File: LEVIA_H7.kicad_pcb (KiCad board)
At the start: 6 copper layers, 36.5 x 36.5 mm, 145 parts, among them J1 TF-028-H265, Q1 AO3400A, SW2 RKCGG140SMTRLFS, U1 USBLC6-2P6, U10 ZX-SH1.0-4PWT, U11 ZX-SH1.0-3PWT, U12 SIT1051TK/3, U13 ZX-SH1.0-4PWT, U14 ICM-42688-P, U15 ICM-42688-P, U16 DPS368XTSA1, U17 IST8310, U18 ZX-SH1.0-4PWT, U19 ZX-SH1.0-6PWT, U2 STM32H743VIHx, U20 ZX-SH1.0-6PWT, U21 ZX-SH1.0-3PWT, U22 ZX-SH1.0-8PWT, U24 ZX-SH1.0-4PWT, U25 BME680, U3 ZX-SH1.0-4PWT, U4 LMR43620R5RPER, U5 LMR604303SRAKRQ1, U6 AP7361C-33FGE-7, U7 AP7361C-33FGE-7, U8 ZX-SH1.0-4PWT, U9 AT7456ELAH, Y1 8MHz, Y2 XL7EL89COI-111YLC-27M

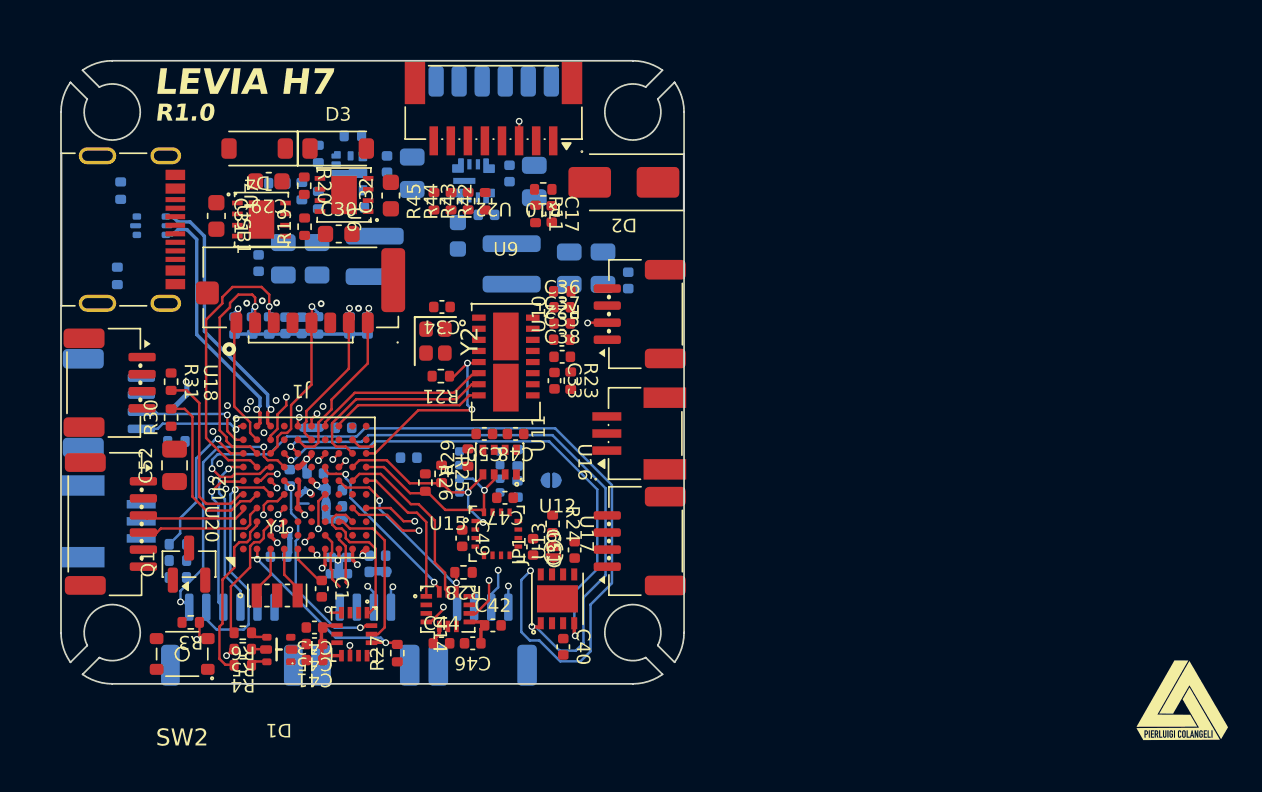
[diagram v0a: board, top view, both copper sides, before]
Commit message: new PCB custom outline
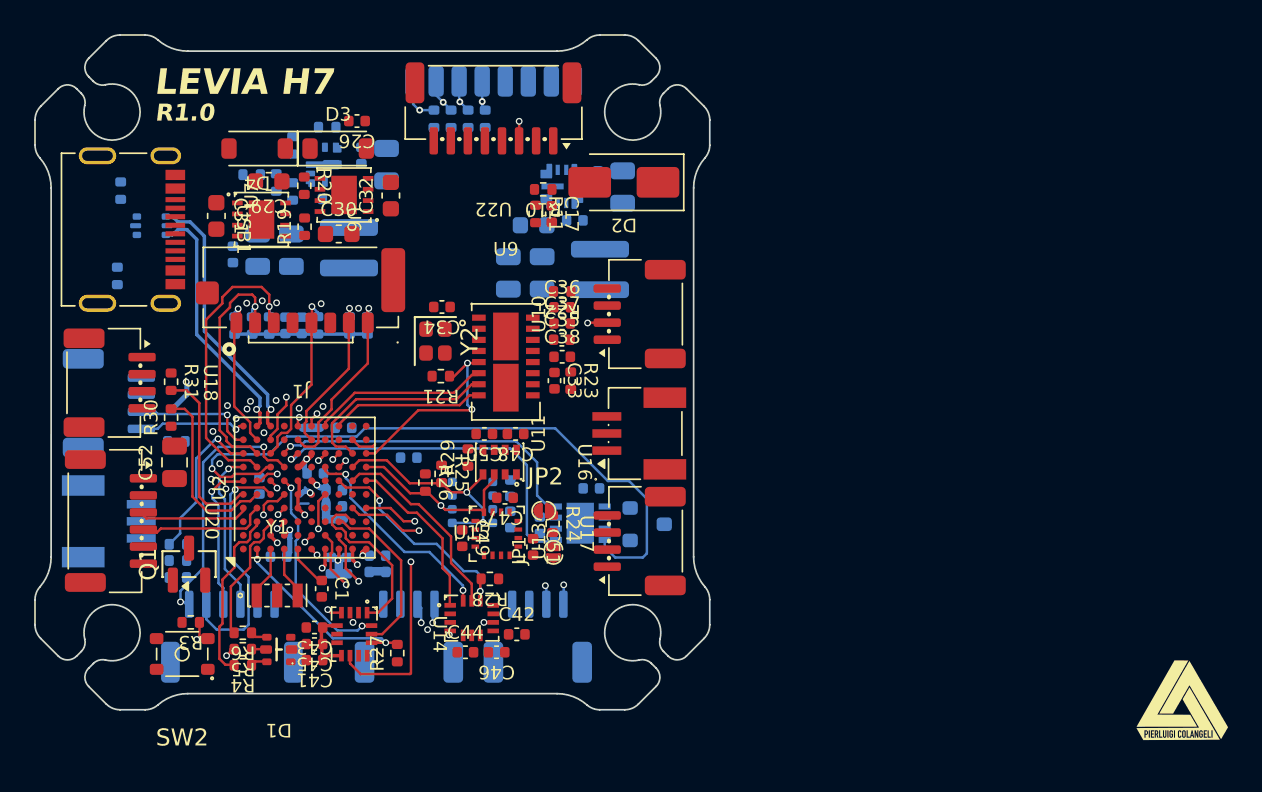
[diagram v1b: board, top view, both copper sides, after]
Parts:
- added D6: PESD2CAN, PCM_Package_TO_SOT_SMD_AKL:SOT-23, B.Cu at (154.8, 78.0)
- C26, JP2: moved to F.Cu
- C39, C40, R42, R43, R44, R45, U12: moved to B.Cu
- moved C26 18.4 mm to (137.8, 54.4), turned to 180 degrees
- moved C40 7.26 mm to (148.5, 78.1)
- moved C22 5.55 mm to (146.7, 63.3)
- moved C13 5.19 mm to (153.4, 58.3)
- moved L1 5.19 mm to (152.0, 63.1)
- moved U4 5.19 mm to (149.8, 58.2)
- moved C15 5.19 mm to (151.9, 57.8)
- moved C20 5.19 mm to (150.6, 60.2)
- moved R42 4.83 mm to (145.3, 54.3), turned to -90 degrees
- moved R44 4.83 mm to (143.3, 54.3), turned to -90 degrees
- moved R45 4.83 mm to (142.3, 54.3), turned to -90 degrees
- moved R43 4.82 mm to (144.3, 54.3), turned to -90 degrees
- moved U12 4.63 mm to (150.9, 77.9), turned to 90 degrees
- moved C18 4.48 mm to (148.2, 60.5), turned to 180 degrees
- moved C39 3.74 mm to (151.5, 75.9), turned to 180 degrees
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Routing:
- net /MCU/MOTOR3: track 3.42 -> 37.2 mm, vias 0 -> 2
- net /MCU/MOTOR4: track 3.13 -> 35.6 mm, vias 0 -> 2
- net /MCU/MOTOR1: track 4.44 -> 35.4 mm, vias 1 -> 2
- net /MCU/MOTOR2: track 3.17 -> 33.5 mm, vias 1 -> 2
- net /CAN/CAN1.TX: track 34.5 -> 20.7 mm, vias 2 -> 1
- net /CAN/CAN1.RX: track 30.0 -> 18.7 mm, vias 2 -> 1
- net /CAN/CAN1.SILENT: track 49.0 -> 38.8 mm, vias 2 -> 1
- net /MCU/GYRO1_CLKIN: track 15.5 -> 19.2 mm
- net +3V3_SENS: track 7.51 -> 4.25 mm
- net /MCU/UART2.RX: track 11.6 -> 14.6 mm
- net /MCU/UART2.TX: track 13.5 -> 16.5 mm
- net /MCU/UART6.RX: track 18.3 -> 20.8 mm
- net /MCU/SPI4.CS: track 10.9 -> 13.2 mm
- net /MCU/SPI4.MOSI: track 10.7 -> 12.6 mm
- net /MCU/I2C2.SCL: track 12.3 -> 13.6 mm
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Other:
- board size 36.5 x 36.5 mm -> 39.5 x 39.5 mm

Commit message: save
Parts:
- added REF**: KiCad-Logo2_5mm_SilkScreen, Symbol:KiCad-Logo2_5mm_SilkScreen, B.Cu at (139.1, 70.4)
- added REF**: OSHW-Logo_5.7x6mm_SilkScreen, Symbol:OSHW-Logo_5.7x6mm_SilkScreen, B.Cu at (129.4, 54.0)
- R42, R43, R44, R45: moved to F.Cu
- moved JP1 4.44 mm to (151.1, 75.6), turned to -90 degrees
- moved U11 3.40 mm to (154.6, 69.3)
- moved C13 2.90 mm to (150.5, 58.3)
- moved C15 2.90 mm to (149.0, 57.8)
- moved C18 2.90 mm to (145.3, 60.5)
- moved C20 2.90 mm to (147.7, 60.2)
- moved C22 2.90 mm to (143.8, 63.3)
- moved C24 2.90 mm to (145.8, 63.3)
- moved L1 2.90 mm to (149.1, 63.1)
- moved U4 2.90 mm to (146.9, 58.2)
- moved R44 2.75 mm to (142.7, 56.9), turned to 90 degrees
- moved R45 2.75 mm to (141.7, 56.9), turned to 90 degrees
- moved R42 2.75 mm to (144.7, 56.9), turned to 90 degrees
- moved R43 2.75 mm to (143.7, 56.9), turned to 90 degrees
- moved U10 2.61 mm to (154.6, 63.1)
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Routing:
- net /MCU/UART8.RX: track 43.5 -> 34.8 mm, vias 1 -> 2
- net /MCU/MOTOR2: track 33.5 -> 41.2 mm
- net /MCU/MOTOR1: track 35.4 -> 42.9 mm
- net /MCU/UART2.RX: track 14.6 -> 22.0 mm
- net /MCU/UART2.TX: track 16.5 -> 23.9 mm
- net /MCU/MOTOR3: track 37.2 -> 42.7 mm
- net /MCU/MOTOR4: track 35.6 -> 41.0 mm
- net +5V_SYS: track 0.00 -> 5.02 mm
- net /MCU/ADC1_VBAT1: track 48.9 -> 44.7 mm, vias 1 -> 2
- net Net-(U9-CLKIN): track 0.00 -> 3.38 mm
- net /ANALOG VTX/UART1.TX: track 23.5 -> 26.3 mm
- net /I2C1|SPI3/I2C1.SCL: track 10.6 -> 13.0 mm
- net /I2C1|SPI3/I2C1.SDA: track 10.4 -> 12.6 mm
- net Net-(U9-XFB): track 0.00 -> 2.05 mm
- net Net-(C36-Pad2): track 0.00 -> 2.03 mm
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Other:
- board text removed: "ADCs"
- board text removed: "BOOT"
- board text removed: "BUZZ"
- board text removed: "CAN-FD"
- board text removed: "DIGI VTX"
- board text removed: "I2C/SPI"
- board text removed: "JTAG"
- board text removed: "LDOS"
- board text removed: "LEDS"
- board text removed: "MOTORS"
- board text removed: "OSD"
- board text removed: "S E N S O R S"
- board text removed: "SD-CARD"
- board text removed: "SWITCHING REGS"
- board text removed: "UARTS"
- board text removed: "VTX"

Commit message: power routing
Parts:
- removed NT2, NT3, NT4, NT5: NetTie_2, NetTie:NetTie-2_SMD_Pad0.5mm
- added FB1: 600Ω@100MHz, Inductor_SMD:L_0402_1005Metric, B.Cu at (137.8, 80.1)
- added TP11: TestPoint, TestPoint:TestPoint_Pad_D1.0mm, B.Cu at (134.3, 75.5)
- R42, R43, R44, R45: moved to B.Cu
- moved NT1 24.8 mm to (128.3, 58.4)
- moved C9 5.24 mm to (136.5, 77.1), turned to 0 degrees
- moved C2 3.37 mm to (137.6, 78.0), turned to 180 degrees
- moved R42 1.91 mm to (144.7, 55.0)
- moved R43 1.91 mm to (143.7, 55.0)
- moved R44 1.91 mm to (142.7, 55.0)
- moved R45 1.91 mm to (141.7, 55.0)
- moved C12 1.90 mm to (133.7, 76.8), turned to 180 degrees
- moved C4 1.82 mm to (137.6, 78.9), turned to 180 degrees
- moved C8 1.55 mm to (136.1, 73.6)
- moved C5 1.55 mm to (136.2, 78.9), turned to 90 degrees
- moved C7 1.48 mm to (137.9, 76.3), turned to -90 degrees
- moved C3 1.06 mm to (136.2, 80.7)
- moved C6 0.97 mm to (134.0, 79.3), turned to -90 degrees
- moved C10 0.80 mm to (136.5, 76.2)
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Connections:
- net /MCU/VCAP renamed VCAP
- net /MCU/VDDA renamed VDDA
- C10 pad 1: /MCU/VDD_USB -> VDD
- C12 pad 1: /MCU/VDD_LDO -> VDD
- C2 pad 1: /MCU/VDD -> VDD
- C4 pad 1: /MCU/VDD -> VDD
- C6 pad 1: /MCU/VDD -> VDD
- C7 pad 1: /MCU/VDD_USB -> VDD
- C9 pad 1: /MCU/VDD -> VDD
- NT1 pad 2: /MCU/VDD -> VDD
- TP5 pad 1: /MCU/MOTOR1 -> /MOTORS[1-4]/S1
- TP6 pad 1: /MCU/MOTOR2 -> /MOTORS[1-4]/S2
- TP7 pad 1: /MCU/MOTOR3 -> /MOTORS[1-4]/S3
- TP8 pad 1: /MCU/MOTOR4 -> /MOTORS[1-4]/S4
- U2 pad D2: /MCU/VDD -> VDD
- U2 pad F4: /MCU/VDD_LDO -> VDD
- U2 pad F5: /MCU/VDD -> VDD
- U2 pad F6: /MCU/VDD_USB -> VDD
- U2 pad F7: unconnected-(U2A-PDR_ON-PadF7) -> Net-(U2A-PDR_ON)
- U2 pad K1: /MCU/VDD -> VDD
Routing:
- net VDD: track 0.00 -> 51.8 mm, vias 0 -> 6
- net /DIGITAL VTX/UART3.RX: track 1.55 -> 25.9 mm, vias 0 -> 2
- net /MCU/VDD: track 12.8 -> 0.00 mm, vias 3 -> 0
- net /MOTORS[1-4]/S4: track 0.00 -> 5.02 mm, vias 0 -> 1
- net /MOTORS[1-4]/S3: track 0.00 -> 4.77 mm, vias 0 -> 1
- net /MCU/UART8.RX: track 34.8 -> 39.5 mm, vias 2 -> 3
- net /MOTORS[1-4]/S2: track 0.00 -> 4.65 mm, vias 0 -> 1
- net /MOTORS[1-4]/S1: track 0.00 -> 4.51 mm, vias 0 -> 1
- net +3V3_MCU: track 14.0 -> 9.74 mm, vias 2 -> 3
- net /MCU/MOTOR4: track 41.0 -> 43.7 mm
- net /MCU/MOTOR1: track 42.9 -> 45.6 mm
- net /MCU/MOTOR3: track 42.7 -> 45.4 mm
- net /MCU/SPI1.MOSI: track 12.3 -> 14.9 mm
- net /MCU/MOTOR2: track 41.2 -> 43.8 mm
- net /MCU/VDD_USB: track 2.55 -> 0.00 mm, vias 1 -> 0
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- added copper zone on B.Cu, net GND
- added copper zone on F.Cu, net GND
- added copper zone on In1.Cu, net GND
- added copper zone on In2.Cu, net GND
- added copper zone on In3.Cu, net GND
- added copper zone on In4.Cu, net GND
- added copper zone on In2.Cu, net VDD

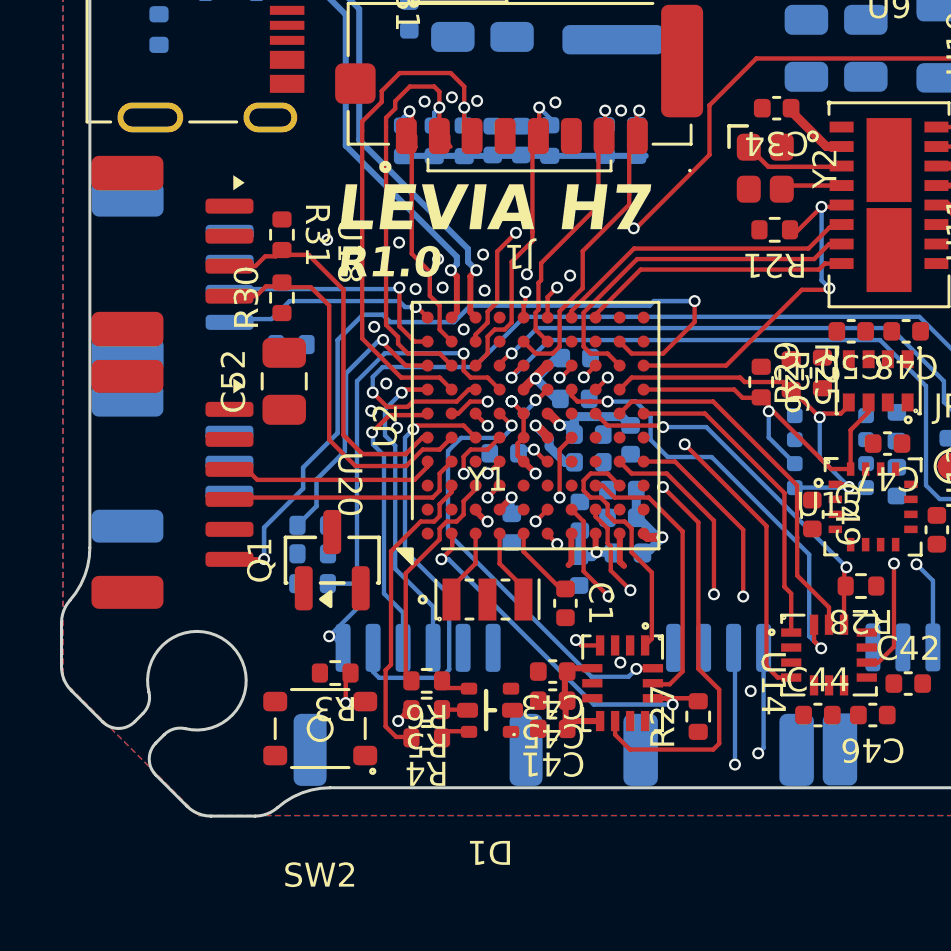
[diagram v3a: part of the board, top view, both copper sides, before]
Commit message: better gnd pour
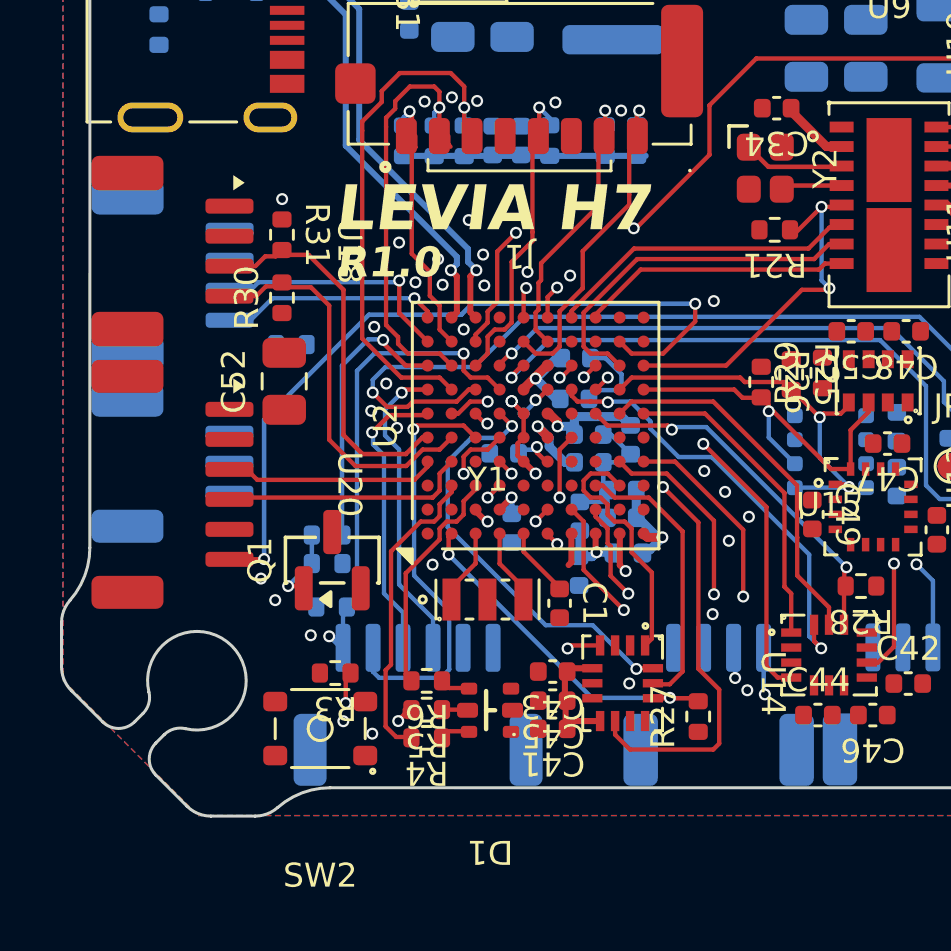
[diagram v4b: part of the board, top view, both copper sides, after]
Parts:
- moved R32 1.01 mm to (128.0, 81.9)
- moved R34 0.58 mm to (127.8, 79.5), turned to 180 degrees
- moved R35 0.58 mm to (127.8, 80.5), turned to 0 degrees
- moved C1 0.19 mm to (135.6, 81.8)
- moved U3 0.07 mm to (122.9, 70.8)
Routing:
- net GND: track 5.78 -> 14.2 mm, vias 24 -> 39
- net /MCU/UART2.RX: track 22.9 -> 16.0 mm
- net /MCU/UART2.TX: track 24.1 -> 19.7 mm
- net /MCU/9V_EN: track 26.4 -> 23.8 mm
- net Net-(Q1-G): track 0.95 -> 2.60 mm, vias 0 -> 1
- net /MCU/SPI1.CS: track 13.0 -> 12.2 mm
- net /MCU/SPI1.MOSI: track 14.9 -> 14.3 mm
- net +3V3_MCU: vias 3 -> 2
